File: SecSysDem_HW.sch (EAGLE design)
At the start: 48 parts, among them Q1 2N3904, T1 MOSFET_NCHANNEL_ENHANCEMENT2N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, T2 MOSFET_NCHANNEL_ENHANCEMENT2N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, T3 MOSFET_NCHANNEL_ENHANCEMENT2N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, U1 XPLAINED_MINI_PINOUT, U2 PCF8574_IO_EXPANDER, U3 MCP4706_DAC, U4 FT24C512A, X1 C-GRID-06-70553, X5 C-GRID-02-70543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

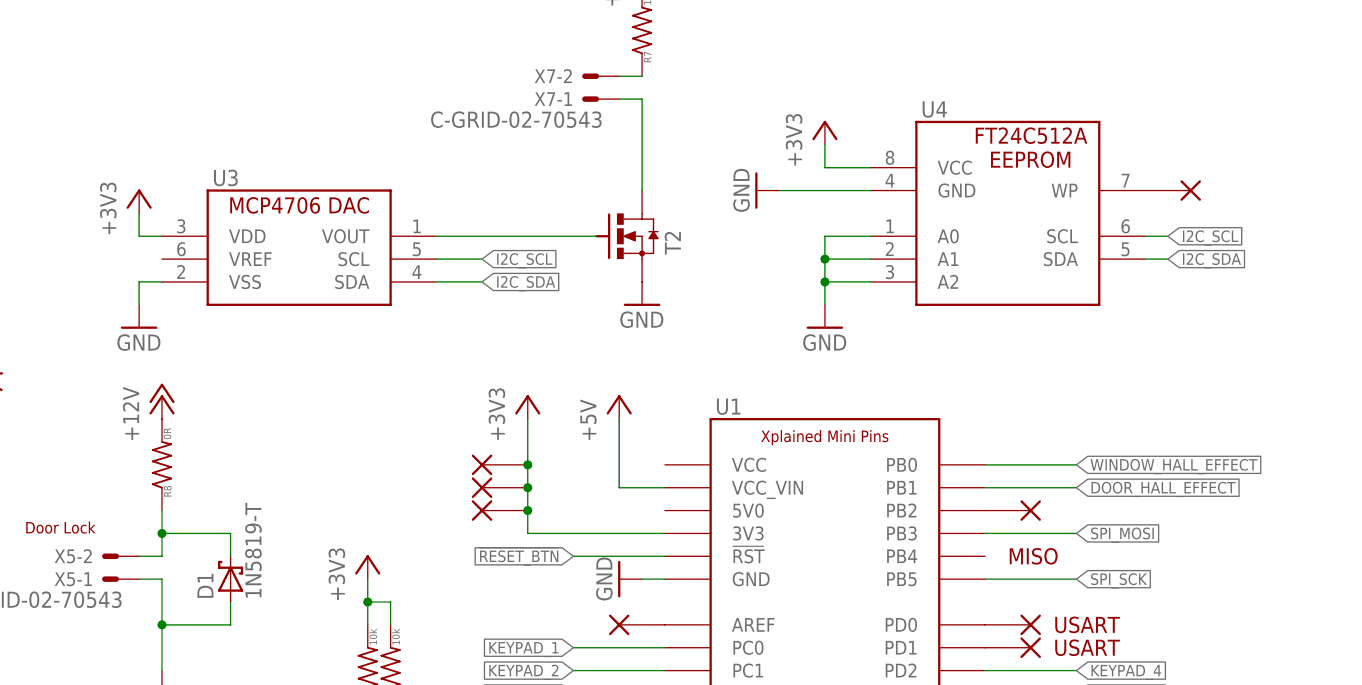
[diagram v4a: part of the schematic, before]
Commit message: Changed DAC to MCP4901-E/SN because the package was too small.
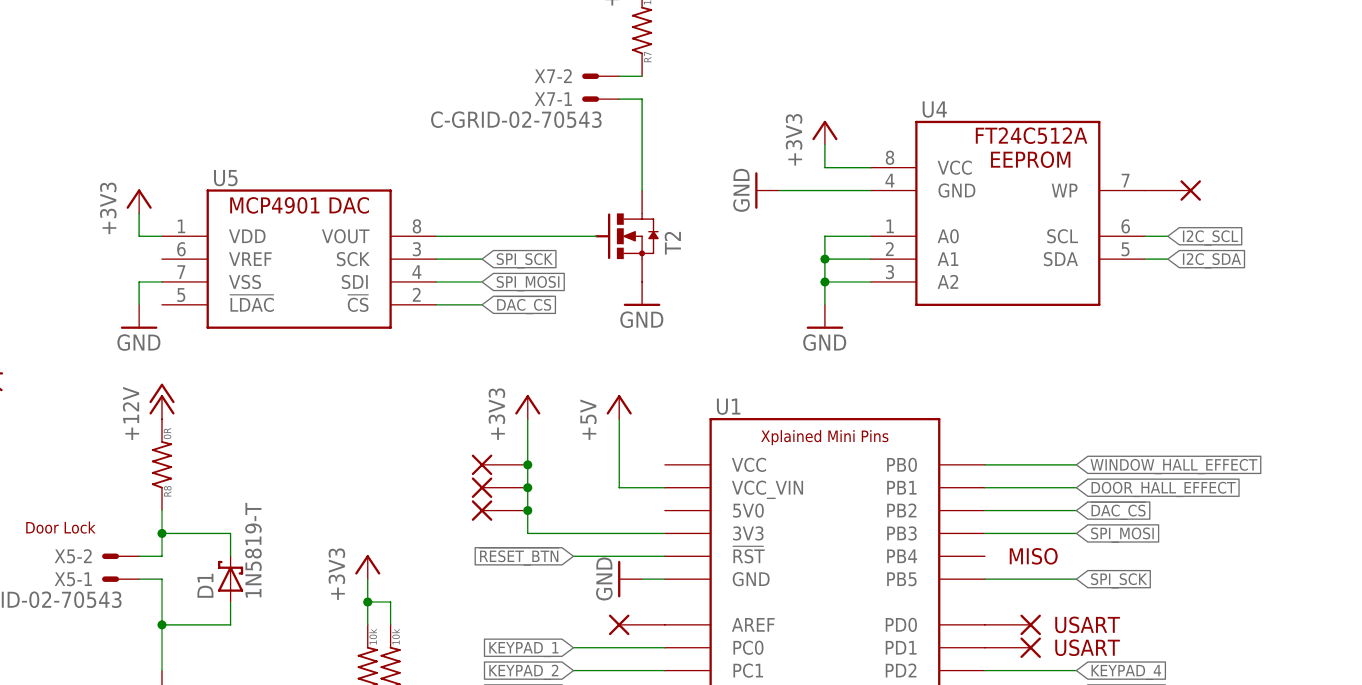
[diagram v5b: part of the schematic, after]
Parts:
- removed U3: MCP4706_DAC, Luke:MCP4706_DAC
- removed V2: PB2, Luke:VIA1
- added U5: MCP4901-E/SN, Luke:MCP4901-E/SN
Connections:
- removed net N$12: U1.PB2, V2.P$1
- new net !DAC_CS: U1.PB2, U5.!CS
- net +3V3: now also U5.VDD; no longer U3.VDD
- net GND: now also U5.VSS; no longer U3.VSS
- net I2C_SCL: no longer U3.SCL
- net I2C_SDA: no longer U3.SDA
- net N$3: now also U5.VOUT; no longer U3.VOUT
- net SPI_MOSI: now also U5.SDI
- net SPI_SCK: now also U5.SCK
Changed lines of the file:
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@@
 <part name="R6" library="Luke" deviceset="RESISTOR" device="0805" value="2.2k"/>
 <part name="GND16" library="supply1" deviceset="GND" device=""/>
-<part name="U3" library="Luke" deviceset="MCP4706_DAC" device=""/>
 <part name="GND17" library="supply1" deviceset="GND" device=""/>
 <part name="+3V7" library="supply1" deviceset="+3V3" device=""/>
@@
 <part name="R9" library="Luke" deviceset="RESISTOR" device="0805" value="0R"/>
 <part name="+3V10" library="supply1" deviceset="+3V3" device=""/>
-<part name="V2" library="Luke" deviceset="VIA1" device="" value="PB2"/>
 <part name="V3" library="Luke" deviceset="VIA1" device="" value="TXD"/>
 <part name="V4" library="Luke" deviceset="VIA1" device="" value="RXD"/>
@@
 <part name="JP6" library="SparkFun-Connectors" deviceset="M04" device="PTH"/>
 <part name="JP7" library="SparkFun-Connectors" deviceset="M07" device=""/>
+<part name="U5" library="Luke" deviceset="MCP4901" device="-E/SN"/>
 </parts>
 <sheets>
@@
 <instance part="R6" gate="G$1" x="213.36" y="149.86"/>
 <instance part="GND16" gate="1" x="205.74" y="149.86" rot="R270"/>
-<instance part="U3" gate="G$1" x="55.88" y="116.84"/>
 <instance part="GND17" gate="1" x="48.26" y="114.3"/>
 <instance part="+3V7" gate="G$1" x="48.26" y="129.54"/>
@@
 <instance part="R9" gate="G$1" x="172.72" y="43.18" rot="R90"/>
 <instance part="+3V10" gate="G$1" x="172.72" y="53.34"/>
-<instance part="V2" gate="G$1" x="147.32" y="93.98"/>
 <instance part="V3" gate="G$1" x="147.32" y="81.28"/>
 <instance part="V4" gate="G$1" x="147.32" y="78.74"/>
@@
 <instance part="JP6" gate="G$1" x="228.6" y="124.46" rot="R180"/>
 <instance part="JP7" gate="G$1" x="231.14" y="101.6" rot="R180"/>
+<instance part="U5" gate="G$1" x="55.88" y="114.3"/>
 </instances>
 <busses>
@@
 </segment>
 <segment>
-<pinref part="U3" gate="G$1" pin="VSS"/>
 <wire x1="50.8" y1="119.38" x2="48.26" y2="119.38" width="0.1524" layer="91"/>
 <wire x1="48.26" y1="119.38" x2="48.26" y2="116.84" width="0.1524" layer="91"/>
 <pinref part="GND17" gate="1" pin="GND"/>
+<pinref part="U5" gate="G$1" pin="VSS"/>
 </segment>
 <segment>
@@
 </segment>
 <segment>
-<pinref part="U3" gate="G$1" pin="SDA"/>
-<wire x1="81.28" y1="119.38" x2="86.36" y2="119.38" width="0.1524" layer="91"/>
-<label x="86.36" y="119.38" size="1.27" layer="95" xref="yes"/>
-</segment>
-<segment>
 <pinref part="U4" gate="G$1" pin="SDA"/>
 <wire x1="160.02" y1="121.92" x2="162.56" y2="121.92" width="0.1524" layer="91"/>
@@
 <pinref part="X1" gate="-4" pin="S"/>
 <wire x1="215.9" y1="71.12" x2="210.82" y2="71.12" width="0.1524" layer="91"/>
-</segment>
-<segment>
-<pinref part="U3" gate="G$1" pin="SCL"/>
-<wire x1="81.28" y1="121.92" x2="86.36" y2="121.92" width="0.1524" layer="91"/>
-<label x="86.36" y="121.92" size="1.27" layer="95" xref="yes"/>
 </segment>
 <segment>
@@
 <label x="127" y="10.16" size="1.27" layer="95" xref="yes"/>
 </segment>
+<segment>
+<pinref part="U5" gate="G$1" pin="SCK"/>
+<wire x1="81.28" y1="121.92" x2="86.36" y2="121.92" width="0.1524" layer="91"/>
+<label x="86.36" y="121.92" size="1.27" layer="95" xref="yes"/>
+</segment>
 </net>
 <net name="SPI_MOSI" class="0">
@@
 <wire x1="124.46" y1="12.7" x2="127" y2="12.7" width="0.1524" layer="91"/>
 <label x="127" y="12.7" size="1.27" layer="95" xref="yes"/>
+</segment>
+<segment>
+<pinref part="U5" gate="G$1" pin="SDI"/>
+<wire x1="81.28" y1="119.38" x2="86.36" y2="119.38" width="0.1524" layer="91"/>
+<label x="86.36" y="119.38" size="1.27" layer="95" xref="yes"/>
 </segment>
 </net>
@@
 </segment>
 <segment>
-<pinref part="U3" gate="G$1" pin="VDD"/>
 <wire x1="50.8" y1="124.46" x2="48.26" y2="124.46" width="0.1524" layer="91"/>
 <wire x1="48.26" y1="124.46" x2="48.26" y2="127" width="0.1524" layer="91"/>
 <pinref part="+3V7" gate="G$1" pin="+3V3"/>
+<pinref part="U5" gate="G$1" pin="VDD"/>
 </segment>
 <segment>
@@
 <net name="N$3" class="0">
 <segment>
-<pinref part="U3" gate="G$1" pin="VOUT"/>
 <wire x1="81.28" y1="124.46" x2="99.06" y2="124.46" width="0.1524" layer="91"/>
 <pinref part="T2" gate="G$1" pin="G"/>
+<pinref part="U5" gate="G$1" pin="VOUT"/>
 </segment>
 </net>
@@
 <pinref part="U4" gate="G$1" pin="WP"/>
 <pinref part="V1" gate="G$1" pin="P$1"/>
-</segment>
-</net>
-<net name="N$12" class="0">
-<segment>
-<pinref part="U1" gate="G$1" pin="PB2"/>
-<pinref part="V2" gate="G$1" pin="P$1"/>
 </segment>
 </net>
@@
 </segment>
 </net>
+<net name="!DAC_CS" class="0">
+<segment>
+<pinref part="U5" gate="G$1" pin="!CS"/>
+<wire x1="81.28" y1="116.84" x2="86.36" y2="116.84" width="0.1524" layer="91"/>
+<label x="86.36" y="116.84" size="1.27" layer="95" xref="yes"/>
+</segment>
+<segment>
+<pinref part="U1" gate="G$1" pin="PB2"/>
+<wire x1="142.24" y1="93.98" x2="152.4" y2="93.98" width="0.1524" layer="91"/>
+<label x="152.4" y="93.98" size="1.27" layer="95" xref="yes"/>
+</segment>
+</net>

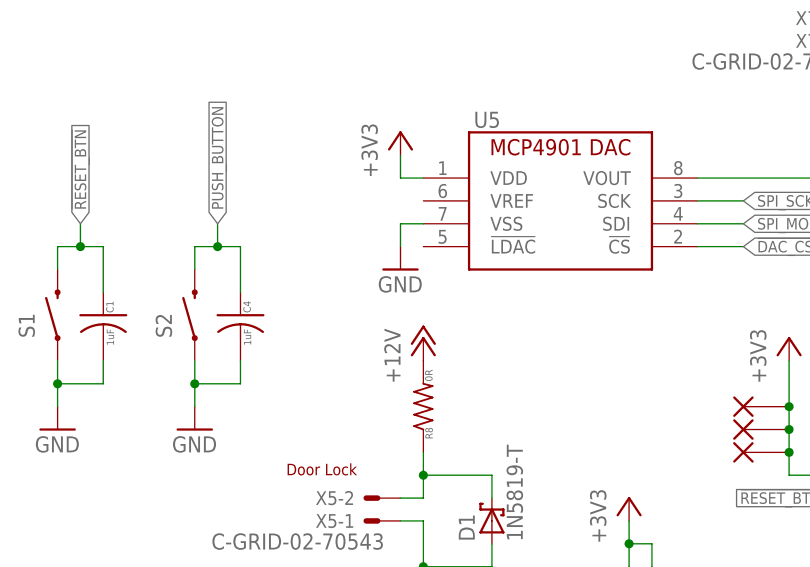
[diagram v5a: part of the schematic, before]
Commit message: Continued board layout. Most components in proper place. No traces yet.
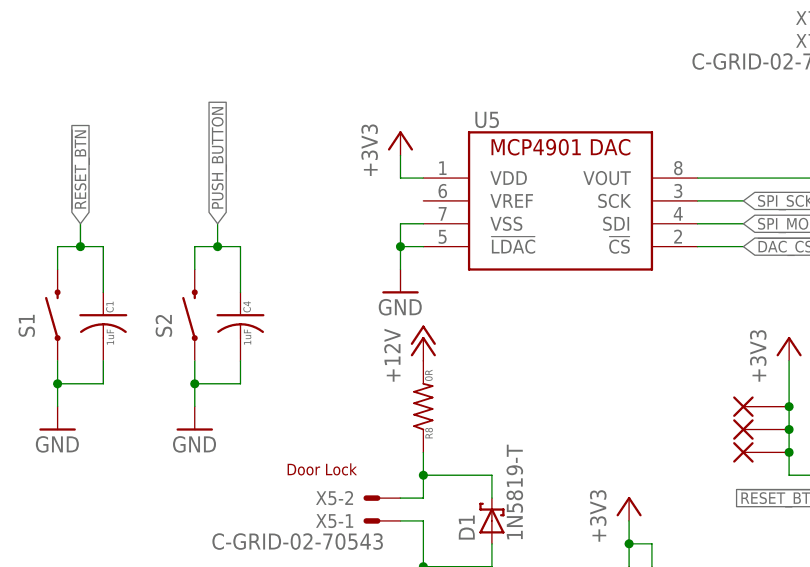
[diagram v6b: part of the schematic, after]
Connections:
- net GND: now also U5.!LDAC
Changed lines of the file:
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@@
 <instance part="R6" gate="G$1" x="213.36" y="149.86"/>
 <instance part="GND16" gate="1" x="205.74" y="149.86" rot="R270"/>
-<instance part="GND17" gate="1" x="48.26" y="114.3"/>
+<instance part="GND17" gate="1" x="48.26" y="111.76"/>
 <instance part="+3V7" gate="G$1" x="48.26" y="129.54"/>
 <instance part="T2" gate="G$1" x="104.14" y="124.46"/>
@@
 <pinref part="GND17" gate="1" pin="GND"/>
 <pinref part="U5" gate="G$1" pin="VSS"/>
+<pinref part="U5" gate="G$1" pin="!LDAC"/>
+<wire x1="48.26" y1="116.84" x2="48.26" y2="114.3" width="0.1524" layer="91"/>
+<wire x1="50.8" y1="116.84" x2="48.26" y2="116.84" width="0.1524" layer="91"/>
+<junction x="48.26" y="116.84"/>
 </segment>
 <segment>

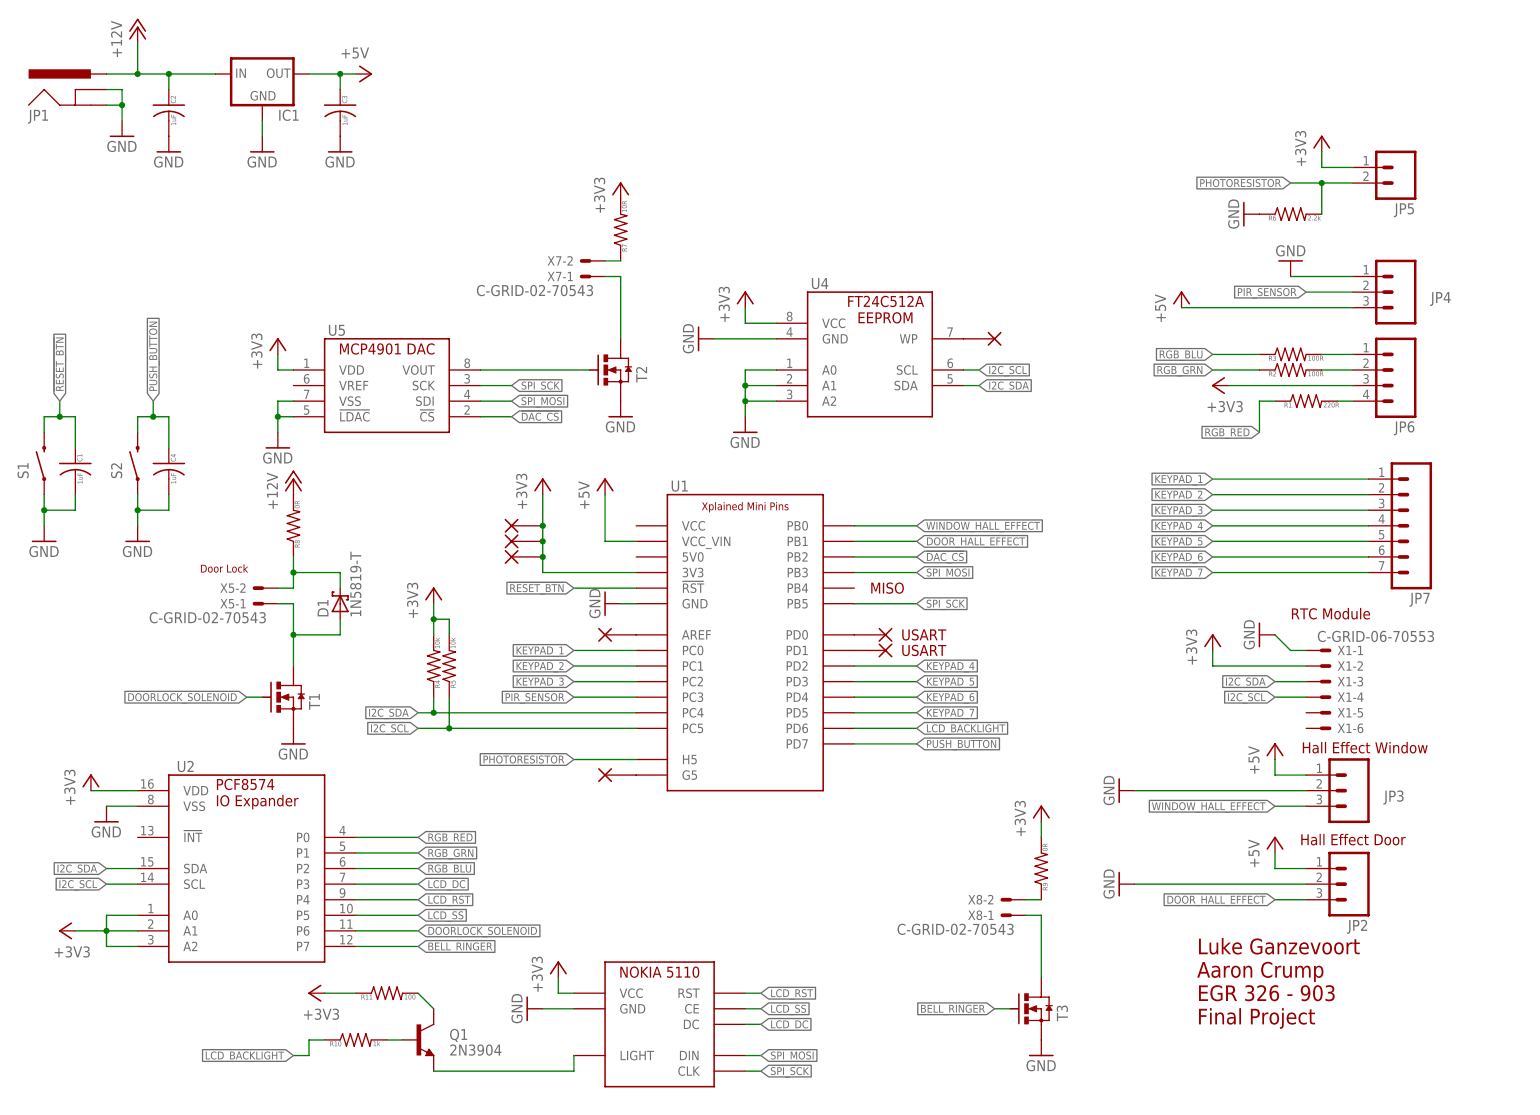
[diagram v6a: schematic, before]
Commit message: Switched IO expander pins to be keypad pins.
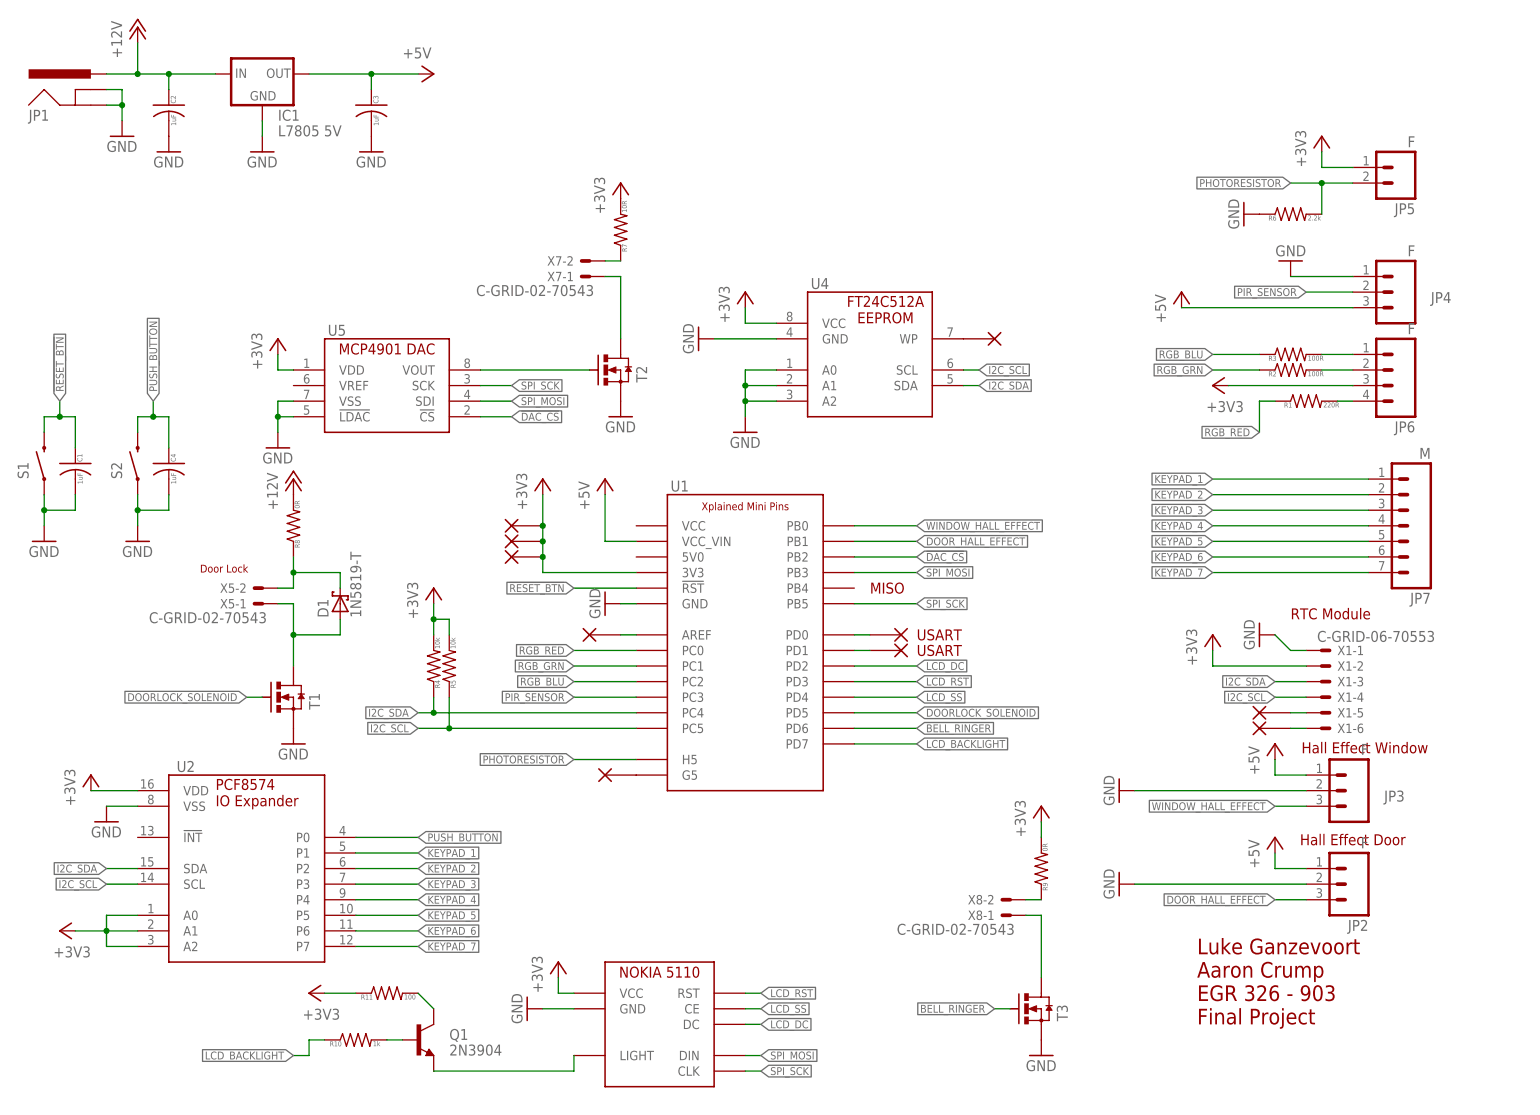
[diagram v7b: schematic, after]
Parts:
- added V10: SQW, Luke:VIA1
- added V2: 32k, Luke:VIA1
- IC1: value (none) -> L7805 5V
- JP2, JP3, JP4, JP5, JP6: value (none) -> F
- JP7: value (none) -> M
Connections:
- new net N$12: V2.P$1, X1-6.S
- new net N$20: V10.P$1, X1-5.S
- net BELL_RINGER: now also U1.PD6; no longer U2.P7
- net DOORLOCK_SOLENOID: now also U1.PD5; no longer U2.P6
- net KEYPAD_1: now also U2.P1; no longer U1.PC0
- net KEYPAD_2: now also U2.P2; no longer U1.PC1
- net KEYPAD_3: now also U2.P3; no longer U1.PC2
- net KEYPAD_4: now also U2.P4; no longer U1.PD2
- net KEYPAD_5: now also U2.P5; no longer U1.PD3
- net KEYPAD_6: now also U2.P6; no longer U1.PD4
- net KEYPAD_7: now also U2.P7; no longer U1.PD5
- net LCD_BACKLIGHT: now also U1.PD7; no longer U1.PD6
- net LCD_DC: now also U1.PD2; no longer U2.P3
- net LCD_RST: now also U1.PD3; no longer U2.P4
- net LCD_SS: now also U1.PD4; no longer U2.P5
- net PUSH_BUTTON: now also U2.P0; no longer U1.PD7
- net RGB_BLU: now also U1.PC2; no longer U2.P2
- net RGB_GRN: now also U1.PC1; no longer U2.P1
- net RGB_RED: now also U1.PC0; no longer U2.P0
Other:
- moved on the sheet: C3
